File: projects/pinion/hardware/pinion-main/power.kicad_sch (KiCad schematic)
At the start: 52 parts, among them J1 PWR1, J2 PWR2, Q1 2N7002, Q2 2N7002, Q3 2N7002, Q4 2N7002, U11 LM73100RPW, U12 LM73100RPW

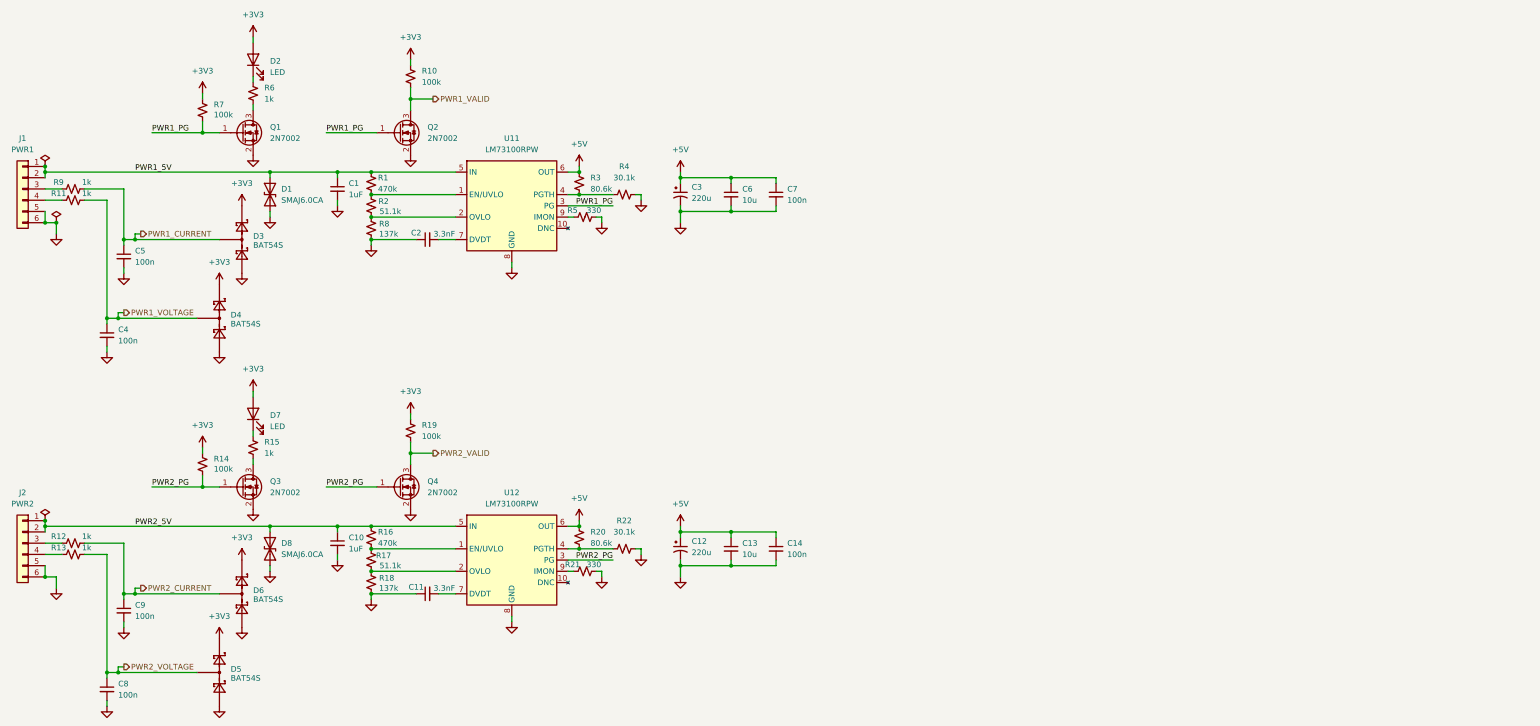
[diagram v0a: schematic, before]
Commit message: [pinion] 3v3 power for sys and fmu
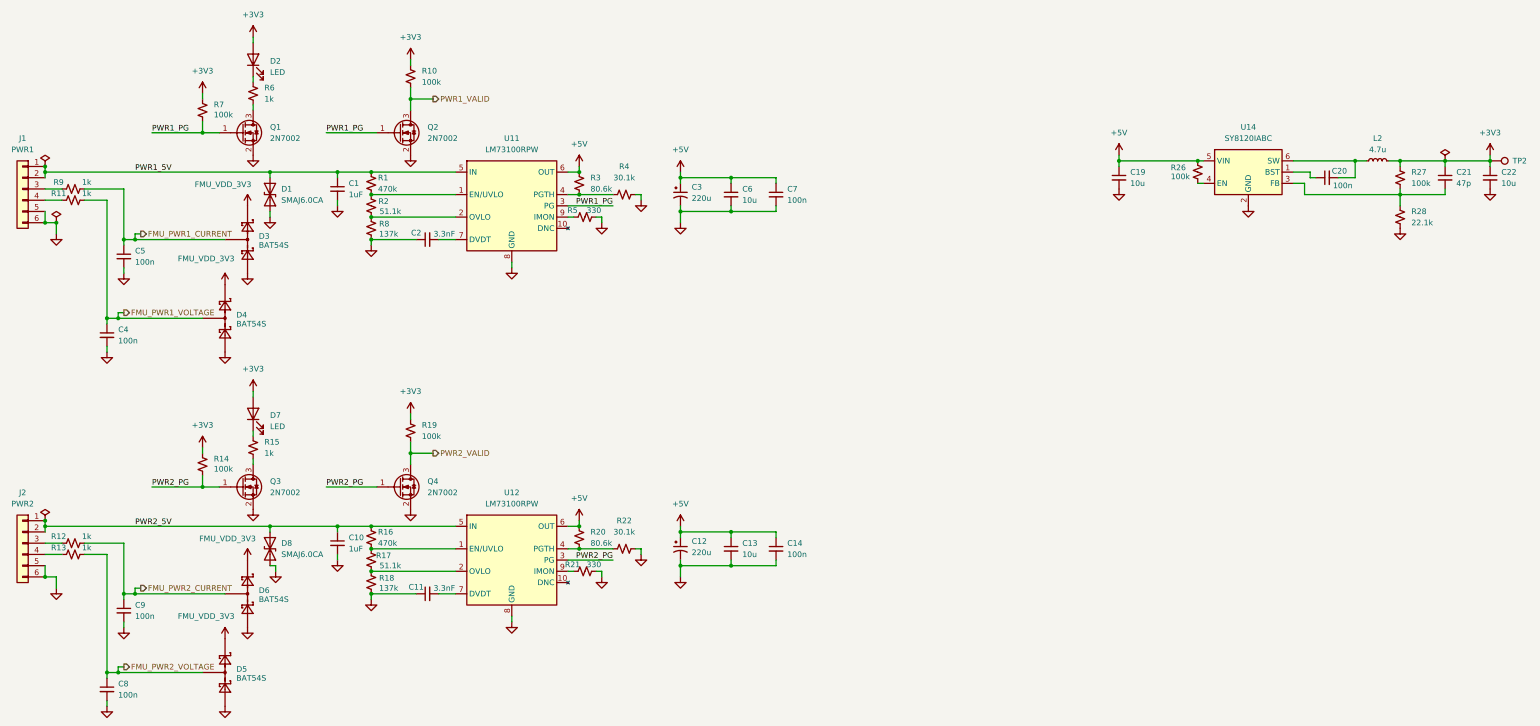
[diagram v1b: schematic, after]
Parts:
- added C19, C22: 10u, Capacitor_SMD:C_0805_2012Metric, symbol Device:C_Small
- added C20: 100n, Capacitor_SMD:C_0402_1005Metric, symbol Device:C_Small
- added C21: 47p, Capacitor_SMD:C_0402_1005Metric, symbol Device:C_Small
- added L2: 4.7u, Inductor_SMD:L_1008_2520Metric, symbol Device:L_Small
- added R26, R27: 100k, Resistor_SMD:R_0402_1005Metric, symbol Device:R_Small_US
- added R28: 22.1k, Resistor_SMD:R_0402_1005Metric, symbol Device:R_Small_US
- added TP2: TestPoint, symbol Connector:TestPoint
- added U14: SY8120IABC, Package_TO_SOT_SMD:SOT-23-6, symbol Regulator_Switching:LGS5116B
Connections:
- net +3V3: now also C21.1, C22.1, L2.2, R27.1, TP2.1; no longer D3.2 (K), D4.2 (K), D5.2 (K), D6.2 (K)
- net +5V: now also C19.1, R26.1, U14.5 (VIN)
- net GND: now also C19.2, C22.2, R28.2, U14.2 (GND)
- net PWR1_CURRENT renamed FMU_PWR1_CURRENT
- net PWR1_VOLTAGE renamed FMU_PWR1_VOLTAGE
- net PWR2_CURRENT renamed FMU_PWR2_CURRENT
- net PWR2_VOLTAGE renamed FMU_PWR2_VOLTAGE
- new net: C20.2, L2.1, U14.6 (SW)
- new net: C21.2, R27.2, R28.1, U14.3 (FB)
- new net: R26.2, U14.4 (EN)
- new net: C20.1, U14.1 (BST)
- new net FMU_VDD_3V3: D3.2 (K), D4.2 (K), D5.2 (K), D6.2 (K)
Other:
- moved on the sheet: D3, D4, D5, D6
